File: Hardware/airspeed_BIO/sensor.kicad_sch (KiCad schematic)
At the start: 4 parts, among them U3 2511020213301

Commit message: set Ilimit and set footprint
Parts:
- added C28, C30: 4.7u, Capacitor_SMD:C_0603_1608Metric, symbol Device:C_Small
- added C29, C31: 0.1u, Capacitor_SMD:C_0603_1608Metric, symbol Device:C_Small
- added TP2: Pressure Vout, TestPoint:TestPoint_Pad_D1.0mm, symbol Connector:TestPoint
- added TP3: GND, TestPoint:TestPoint_Pad_D1.0mm, symbol Connector:TestPoint
- added U6: 2513130810102, TTR:2513130810102_hand, symbol TTR:2513130810102
- added U7: 2525020210002, TTR:2525020210002, symbol TTR:2525020210002
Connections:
- net +3V3: now also C28.1, C29.1, C30.1, C31.1, U6.5 (VDD), U7.3 (VDD)
- net I2C1.SCL: now also U6.1 (SCL), U7.2 (SCL)
- net I2C1.SDA: now also U6.2 (SDA), U7.1 (SDA)
- net GNDA renamed GND
- net GND: now also C28.2, C29.2, C30.2, C31.2, TP3.1, U6.3 (GND), U6.7 (RSVD), U6.8 (RSVD), U7.4 (VSS)
- new net: TP2.1, U6.4 (VOUT)
- no-connect marks 1 -> 2
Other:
- note added: "Differential Pressure"
- note added: "Humidity sensor with integrated temperature sensor"
- note added: "I2C@0X44"
- note added: "I2C@0X78"
- title: (none) -> i2c sensor

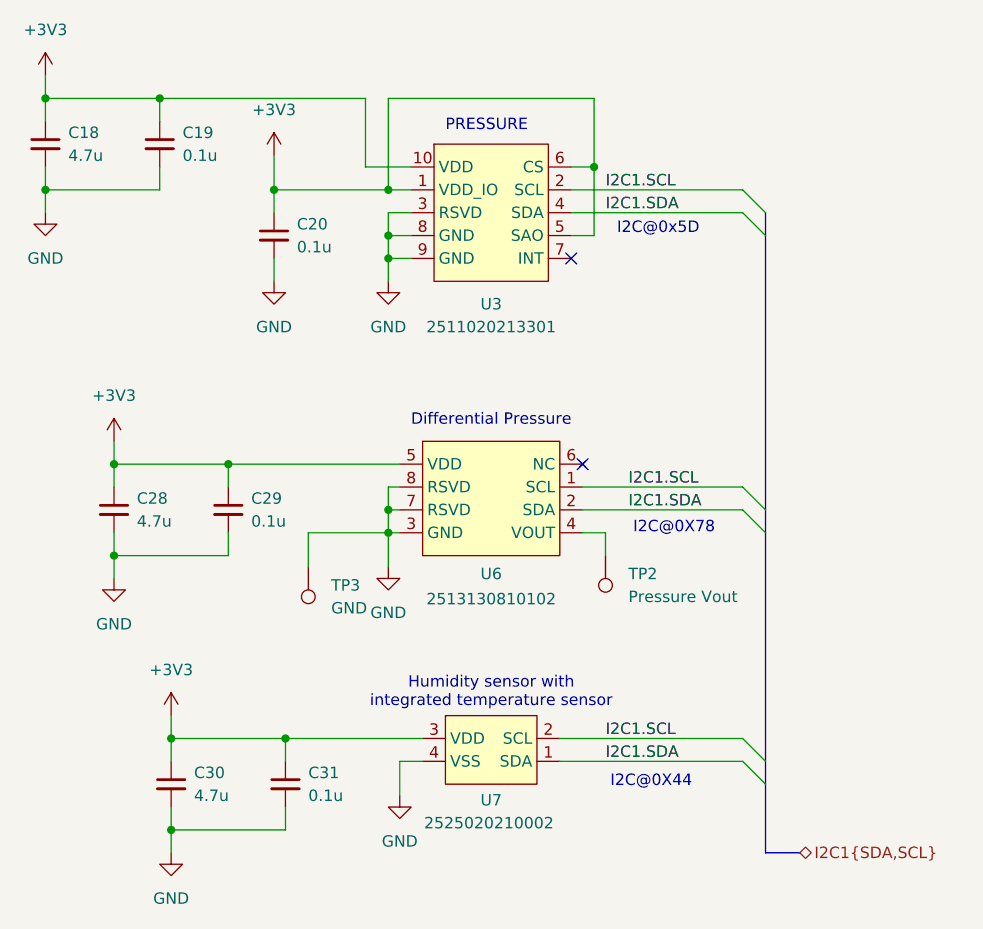
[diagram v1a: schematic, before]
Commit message: layout and fix Schematic
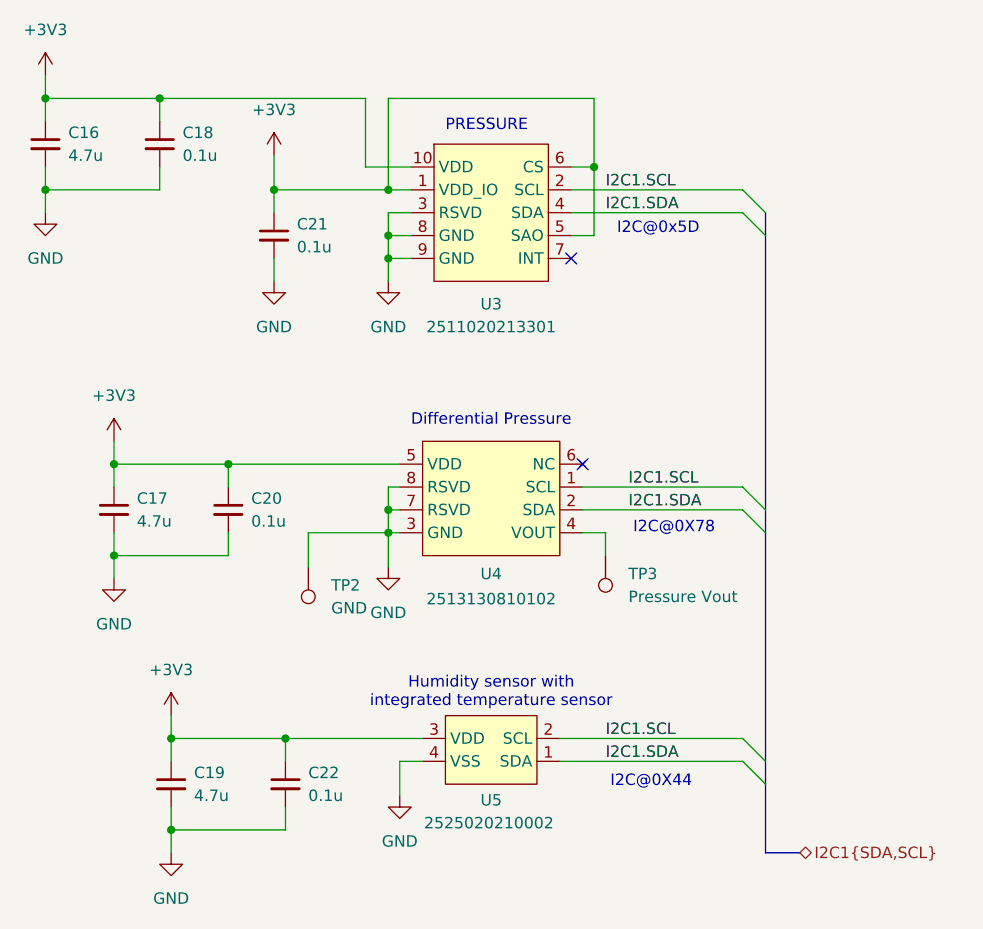
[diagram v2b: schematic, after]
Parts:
- renumbered C18 to C16, C28 to C17, C19 to C18, C30 to C19, C29 to C20, C20 to C21, C31 to C22, TP3 to TP2, TP2 to TP3, U6 to U4, U7 to U5
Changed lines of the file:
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@@
 		(dnp no)
 		(fields_autoplaced yes)
-		(property "Reference" "TP2"
+		(property "Reference" "TP3"
 			(at 152.4 84.5819 0)
 			(effects
@@
 			(project ""
 				(path "/6ddcf4fe-9e51-4114-8222-5fc3f810c12a/aad544ae-2766-4738-957f-ae2f642f67f5"
-					(reference "TP2")
+					(reference "TP3")
 					(unit 1)
 				)
@@
 		(dnp no)
 		(fields_autoplaced yes)
-		(property "Reference" "#PWR048"
+		(property "Reference" "#PWR030"
 			(at 101.6 121.92 0)
 			(effects
@@
 			(project "airspeed_BIO"
 				(path "/6ddcf4fe-9e51-4114-8222-5fc3f810c12a/aad544ae-2766-4738-957f-ae2f642f67f5"
-					(reference "#PWR048")
+					(reference "#PWR030")
 					(unit 1)
 				)
@@
 		(dnp no)
 		(fields_autoplaced yes)
-		(property "Reference" "#PWR022"
+		(property "Reference" "#PWR025"
 			(at 87.63 33.02 0)
 			(effects
@@
 			(project "airspeed_BIO"
 				(path "/6ddcf4fe-9e51-4114-8222-5fc3f810c12a/aad544ae-2766-4738-957f-ae2f642f67f5"
-					(reference "#PWR022")
+					(reference "#PWR025")
 					(unit 1)
 				)
@@
 		(dnp no)
 		(fields_autoplaced yes)
-		(property "Reference" "#PWR024"
+		(property "Reference" "#PWR031"
 			(at 113.03 41.91 0)
 			(effects
@@
 			(project ""
 				(path "/6ddcf4fe-9e51-4114-8222-5fc3f810c12a/aad544ae-2766-4738-957f-ae2f642f67f5"
-					(reference "#PWR024")
+					(reference "#PWR031")
 					(unit 1)
 				)
@@
 		(dnp no)
 		(fields_autoplaced yes)
-		(property "Reference" "C20"
+		(property "Reference" "C21"
 			(at 115.57 45.7262 0)
 			(effects
@@
 			(project "airspeed_BIO"
 				(path "/6ddcf4fe-9e51-4114-8222-5fc3f810c12a/aad544ae-2766-4738-957f-ae2f642f67f5"
-					(reference "C20")
+					(reference "C21")
 					(unit 1)
 				)
@@
 		(dnp no)
 		(fields_autoplaced yes)
-		(property "Reference" "#PWR044"
+		(property "Reference" "#PWR028"
 			(at 95.25 91.44 0)
 			(effects
@@
 			(project "airspeed_BIO"
 				(path "/6ddcf4fe-9e51-4114-8222-5fc3f810c12a/aad544ae-2766-4738-957f-ae2f642f67f5"
-					(reference "#PWR044")
+					(reference "#PWR028")
 					(unit 1)
 				)
@@
 		(dnp no)
 		(fields_autoplaced yes)
-		(property "Reference" "#PWR045"
+		(property "Reference" "#PWR034"
 			(at 125.73 90.17 0)
 			(effects
@@
 			(project "airspeed_BIO"
 				(path "/6ddcf4fe-9e51-4114-8222-5fc3f810c12a/aad544ae-2766-4738-957f-ae2f642f67f5"
-					(reference "#PWR045")
+					(reference "#PWR034")
 					(unit 1)
 				)
@@
 		(dnp no)
 		(fields_autoplaced yes)
-		(property "Reference" "#PWR025"
+		(property "Reference" "#PWR033"
 			(at 125.73 58.42 0)
 			(effects
@@
 			(project "airspeed_BIO"
 				(path "/6ddcf4fe-9e51-4114-8222-5fc3f810c12a/aad544ae-2766-4738-957f-ae2f642f67f5"
-					(reference "#PWR025")
+					(reference "#PWR033")
 					(unit 1)
 				)
@@
 		(on_board yes)
 		(dnp no)
-		(property "Reference" "C30"
+		(property "Reference" "C19"
 			(at 104.14 106.68 0)
 			(effects
@@
 			(project "airspeed_BIO"
 				(path "/6ddcf4fe-9e51-4114-8222-5fc3f810c12a/aad544ae-2766-4738-957f-ae2f642f67f5"
-					(reference "C30")
+					(reference "C19")
 					(unit 1)
 				)
@@
 		(dnp no)
 		(fields_autoplaced yes)
-		(property "Reference" "#PWR023"
+		(property "Reference" "#PWR032"
 			(at 113.03 58.42 0)
 			(effects
@@
 			(project ""
 				(path "/6ddcf4fe-9e51-4114-8222-5fc3f810c12a/aad544ae-2766-4738-957f-ae2f642f67f5"
-					(reference "#PWR023")
+					(reference "#PWR032")
 					(unit 1)
 				)
@@
 		(dnp no)
 		(fields_autoplaced yes)
-		(property "Reference" "#PWR047"
+		(property "Reference" "#PWR029"
 			(at 101.6 104.14 0)
 			(effects
@@
 			(project "airspeed_BIO"
 				(path "/6ddcf4fe-9e51-4114-8222-5fc3f810c12a/aad544ae-2766-4738-957f-ae2f642f67f5"
-					(reference "#PWR047")
+					(reference "#PWR029")
 					(unit 1)
 				)
@@
 		(dnp no)
 		(fields_autoplaced yes)
-		(property "Reference" "TP3"
+		(property "Reference" "TP2"
 			(at 119.38 85.8519 0)
 			(effects
@@
 			(project "airspeed_BIO"
 				(path "/6ddcf4fe-9e51-4114-8222-5fc3f810c12a/aad544ae-2766-4738-957f-ae2f642f67f5"
-					(reference "TP3")
+					(reference "TP2")
 					(unit 1)
 				)
@@
 		(dnp no)
 		(fields_autoplaced yes)
-		(property "Reference" "C19"
+		(property "Reference" "C18"
 			(at 102.87 35.5662 0)
 			(effects
@@
 			(project "airspeed_BIO"
 				(path "/6ddcf4fe-9e51-4114-8222-5fc3f810c12a/aad544ae-2766-4738-957f-ae2f642f67f5"
-					(reference "C19")
+					(reference "C18")
 					(unit 1)
 				)
@@
 		(dnp no)
 		(fields_autoplaced yes)
-		(property "Reference" "C31"
+		(property "Reference" "C22"
 			(at 116.84 106.6862 0)
 			(effects
@@
 			(project "airspeed_BIO"
 				(path "/6ddcf4fe-9e51-4114-8222-5fc3f810c12a/aad544ae-2766-4738-957f-ae2f642f67f5"
-					(reference "C31")
+					(reference "C22")
 					(unit 1)
 				)
@@
 		(on_board yes)
 		(dnp no)
-		(property "Reference" "C28"
+		(property "Reference" "C17"
 			(at 97.79 76.2 0)
 			(effects
@@
 			(project "airspeed_BIO"
 				(path "/6ddcf4fe-9e51-4114-8222-5fc3f810c12a/aad544ae-2766-4738-957f-ae2f642f67f5"
-					(reference "C28")
+					(reference "C17")
 					(unit 1)
 				)
@@
 		(on_board yes)
 		(dnp no)
-		(property "Reference" "U7"
+		(property "Reference" "U5"
 			(at 137.16 109.728 0)
 			(effects
@@
 			(project ""
 				(path "/6ddcf4fe-9e51-4114-8222-5fc3f810c12a/aad544ae-2766-4738-957f-ae2f642f67f5"
-					(reference "U7")
+					(reference "U5")
 					(unit 1)
 				)
@@
 		(dnp no)
 		(fields_autoplaced yes)
-		(property "Reference" "#PWR046"
+		(property "Reference" "#PWR035"
 			(at 127 115.57 0)
 			(effects
@@
 			(project "airspeed_BIO"
 				(path "/6ddcf4fe-9e51-4114-8222-5fc3f810c12a/aad544ae-2766-4738-957f-ae2f642f67f5"
-					(reference "#PWR046")
+					(reference "#PWR035")
 					(unit 1)
 				)
@@
 		(dnp no)
 		(fields_autoplaced yes)
-		(property "Reference" "#PWR043"
+		(property "Reference" "#PWR027"
 			(at 95.25 73.66 0)
 			(effects
@@
 			(project "airspeed_BIO"
 				(path "/6ddcf4fe-9e51-4114-8222-5fc3f810c12a/aad544ae-2766-4738-957f-ae2f642f67f5"
-					(reference "#PWR043")
+					(reference "#PWR027")
 					(unit 1)
 				)
@@
 		(on_board yes)
 		(dnp no)
-		(property "Reference" "C18"
+		(property "Reference" "C16"
 			(at 90.17 35.56 0)
 			(effects
@@
 			(project "airspeed_BIO"
 				(path "/6ddcf4fe-9e51-4114-8222-5fc3f810c12a/aad544ae-2766-4738-957f-ae2f642f67f5"
-					(reference "C18")
+					(reference "C16")
 					(unit 1)
 				)
@@
 		(on_board yes)
 		(dnp no)
-		(property "Reference" "U6"
+		(property "Reference" "U4"
 			(at 137.16 84.582 0)
 			(effects
@@
 			(project ""
 				(path "/6ddcf4fe-9e51-4114-8222-5fc3f810c12a/aad544ae-2766-4738-957f-ae2f642f67f5"
-					(reference "U6")
+					(reference "U4")
 					(unit 1)
 				)
@@
 		(dnp no)
 		(fields_autoplaced yes)
-		(property "Reference" "C29"
+		(property "Reference" "C20"
 			(at 110.49 76.2062 0)
 			(effects
@@
 			(project "airspeed_BIO"
 				(path "/6ddcf4fe-9e51-4114-8222-5fc3f810c12a/aad544ae-2766-4738-957f-ae2f642f67f5"
-					(reference "C29")
-					(unit 1)
-				)
+					(reference "C20")
+					(unit 1)
+				)

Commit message: layoyt end
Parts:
- renumbered C16 to C15, C17 to C16, C18 to C17, C19 to C18, C20 to C19, C21 to C20, C22 to C21, TP2 to TP1, TP3 to TP2
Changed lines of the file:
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@@
 		(dnp no)
 		(fields_autoplaced yes)
-		(property "Reference" "TP3"
+		(property "Reference" "TP2"
 			(at 152.4 84.5819 0)
 			(effects
@@
 			(project ""
 				(path "/6ddcf4fe-9e51-4114-8222-5fc3f810c12a/aad544ae-2766-4738-957f-ae2f642f67f5"
-					(reference "TP3")
+					(reference "TP2")
 					(unit 1)
 				)
@@
 		(dnp no)
 		(fields_autoplaced yes)
-		(property "Reference" "C21"
+		(property "Reference" "C20"
 			(at 115.57 45.7262 0)
 			(effects
@@
 			(project "airspeed_BIO"
 				(path "/6ddcf4fe-9e51-4114-8222-5fc3f810c12a/aad544ae-2766-4738-957f-ae2f642f67f5"
-					(reference "C21")
+					(reference "C20")
 					(unit 1)
 				)
@@
 		(on_board yes)
 		(dnp no)
-		(property "Reference" "C19"
+		(property "Reference" "C18"
 			(at 104.14 106.68 0)
 			(effects
@@
 			(project "airspeed_BIO"
 				(path "/6ddcf4fe-9e51-4114-8222-5fc3f810c12a/aad544ae-2766-4738-957f-ae2f642f67f5"
-					(reference "C19")
+					(reference "C18")
 					(unit 1)
 				)
@@
 		(dnp no)
 		(fields_autoplaced yes)
-		(property "Reference" "TP2"
+		(property "Reference" "TP1"
 			(at 119.38 85.8519 0)
 			(effects
@@
 			(project "airspeed_BIO"
 				(path "/6ddcf4fe-9e51-4114-8222-5fc3f810c12a/aad544ae-2766-4738-957f-ae2f642f67f5"
-					(reference "TP2")
+					(reference "TP1")
 					(unit 1)
 				)
@@
 		(dnp no)
 		(fields_autoplaced yes)
-		(property "Reference" "C18"
+		(property "Reference" "C17"
 			(at 102.87 35.5662 0)
 			(effects
@@
 			(project "airspeed_BIO"
 				(path "/6ddcf4fe-9e51-4114-8222-5fc3f810c12a/aad544ae-2766-4738-957f-ae2f642f67f5"
-					(reference "C18")
+					(reference "C17")
 					(unit 1)
 				)
@@
 		(dnp no)
 		(fields_autoplaced yes)
-		(property "Reference" "C22"
+		(property "Reference" "C21"
 			(at 116.84 106.6862 0)
 			(effects
@@
 			(project "airspeed_BIO"
 				(path "/6ddcf4fe-9e51-4114-8222-5fc3f810c12a/aad544ae-2766-4738-957f-ae2f642f67f5"
-					(reference "C22")
+					(reference "C21")
 					(unit 1)
 				)
@@
 		(on_board yes)
 		(dnp no)
-		(property "Reference" "C17"
+		(property "Reference" "C16"
 			(at 97.79 76.2 0)
 			(effects
@@
 			(project "airspeed_BIO"
 				(path "/6ddcf4fe-9e51-4114-8222-5fc3f810c12a/aad544ae-2766-4738-957f-ae2f642f67f5"
-					(reference "C17")
+					(reference "C16")
 					(unit 1)
 				)
@@
 		(on_board yes)
 		(dnp no)
-		(property "Reference" "C16"
+		(property "Reference" "C15"
 			(at 90.17 35.56 0)
 			(effects
@@
 			(project "airspeed_BIO"
 				(path "/6ddcf4fe-9e51-4114-8222-5fc3f810c12a/aad544ae-2766-4738-957f-ae2f642f67f5"
-					(reference "C16")
+					(reference "C15")
 					(unit 1)
 				)
@@
 		(dnp no)
 		(fields_autoplaced yes)
-		(property "Reference" "C20"
+		(property "Reference" "C19"
 			(at 110.49 76.2062 0)
 			(effects
@@
 			(project "airspeed_BIO"
 				(path "/6ddcf4fe-9e51-4114-8222-5fc3f810c12a/aad544ae-2766-4738-957f-ae2f642f67f5"
-					(reference "C20")
-					(unit 1)
-				)
+					(reference "C19")
+					(unit 1)
+				)
